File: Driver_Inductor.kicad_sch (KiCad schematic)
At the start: 6 parts, among them J1 2-338069-0, J2 DC+, J3 DC-, J4 OUT1, J5 OUT2

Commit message: Тестовая версия
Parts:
- J2, J3: footprint Connector Power:M4 -> Connector_Power:M5
- J4, J5: footprint Connector Power:M5 -> Connector_Power:M5
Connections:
- net Current_N is gone; now on net +15V: J1.8
- net Current_P is gone; now on net GND: J1.7
- net +15V: now also J1.10; no longer J1.18, J1.2
- net DESAT_H: now also D20.25 (DC+), D20.26 (DC+), J2.1 (Pin_1); no longer D20.15 (DC+)
- net E3: no longer D20.21 (OUT2), D20.22 (OUT2), J5.1 (Pin_1)
- net Fault_N: now also J1.1; no longer J1.10
- net Fault_P: now also J1.2; no longer J1.9
- net GND: now also J1.9; no longer J1.1
- net PWM1_N: now also J1.14; no longer J1.16
- net PWM1_P: now also J1.13; no longer J1.15
- net PWM2_N: now also J1.16; no longer J1.14
- net PWM2_P: now also J1.15; no longer J1.13
- net Reset: now also J1.18; no longer J1.20
- net Temp_N: now also J1.11; no longer J1.12
- net Temp_P: now also J1.12; no longer J1.11
- net E1 renamed OUT1
- new net Current: J1.20
- new net OUT2: D20.21 (OUT2), D20.22 (OUT2)
- new net OUT2_Sens: J5.1 (Pin_1)
- no-connect marks 5 -> 6
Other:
- moved on the sheet: J5

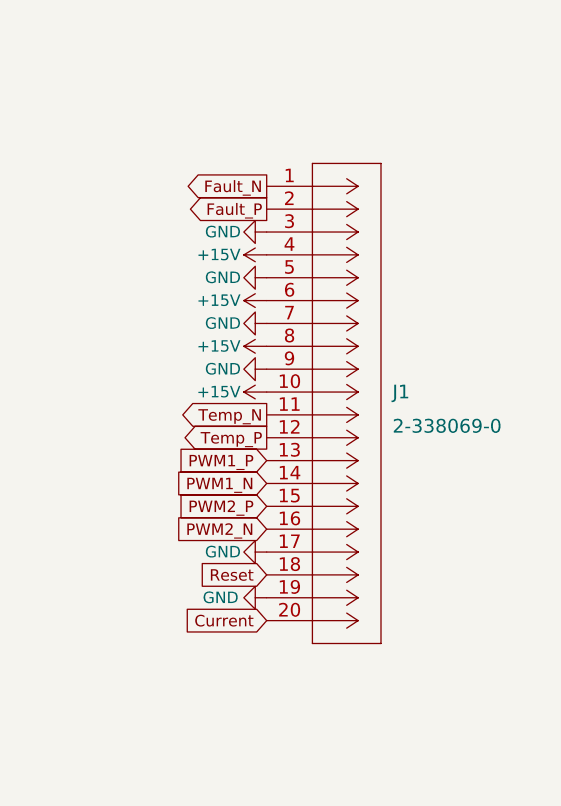
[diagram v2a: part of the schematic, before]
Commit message: Убрал питание 3.3В
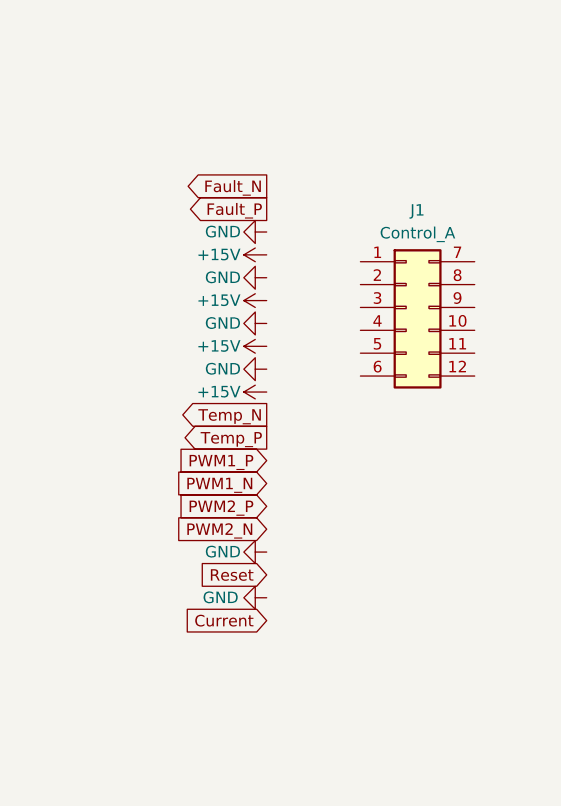
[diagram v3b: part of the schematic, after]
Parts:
- removed J1: 2-338069-0, Connector_My:2-338069-0, symbol Connector_My:2-338069-0
- added J1: Control_A, Connector_Molex:Molex_Micro-Fit_3.0_43045-1212_2x06_P3.00mm_Vertical, symbol Connector_Generic:Conn_02x06_Top_Bottom

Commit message: Развел все дорожки
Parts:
- added C10: 1u, Capacitor_THT:C_Rect_L31.5mm_W13.0mm_P27.50mm_MKS4, symbol Device:C
- J2, J3, J4, J5: footprint Connector_Power:M5 -> Connector_My:Bush_M4
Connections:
- net +15V: now also J1.2 (Pin_2)
- net Current: now also J1.12 (Pin_12)
- net Fault_N: now also J1.10 (Pin_10)
- net Fault_P: now also J1.4 (Pin_4)
- net GND: now also J1.8 (Pin_8)
- net PWM1_N: now also J1.9 (Pin_9)
- net PWM1_P: now also J1.3 (Pin_3)
- net PWM2_N: now also J1.11 (Pin_11)
- net PWM2_P: now also J1.5 (Pin_5)
- net Reset: now also J1.6 (Pin_6)
- net Temp_N: now also J1.1 (Pin_1)
- net Temp_P: now also J1.7 (Pin_7)
- net DC-: now reaches D20.27 (DC-), D20.28 (DC-), J3.1 (Pin_1)
- net DC-: now also C10.2
- net DESAT_H renamed DC+
- net DC+: now also C10.1
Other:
- moved on the sheet: J1, J2, J3

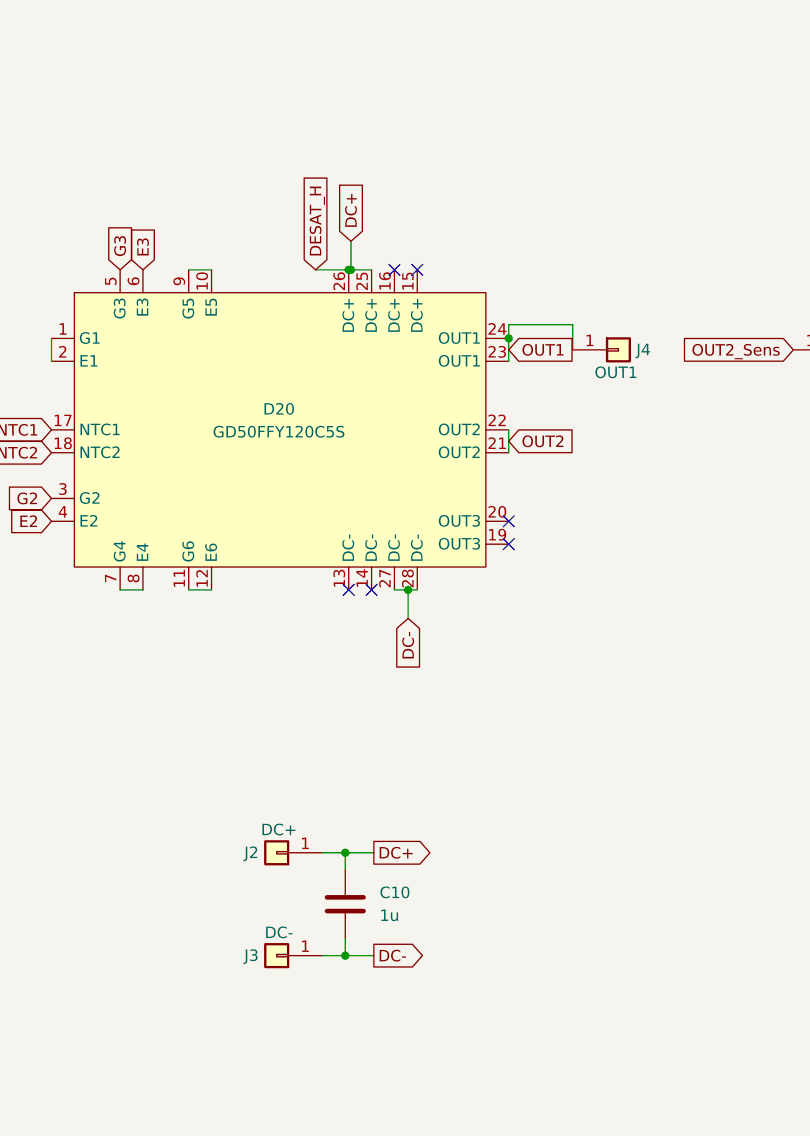
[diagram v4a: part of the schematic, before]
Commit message: Заменил в схеме символы питания
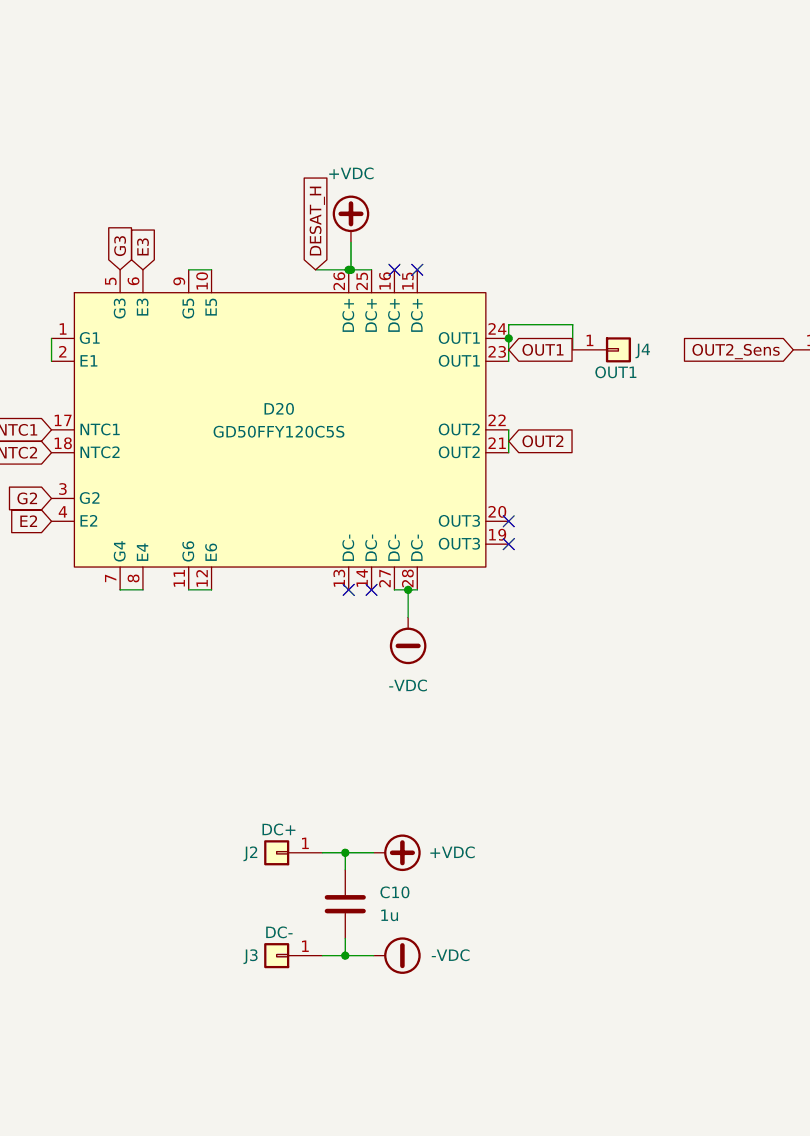
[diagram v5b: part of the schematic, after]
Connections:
- net DC+ renamed +VDC
- net DC- renamed -VDC

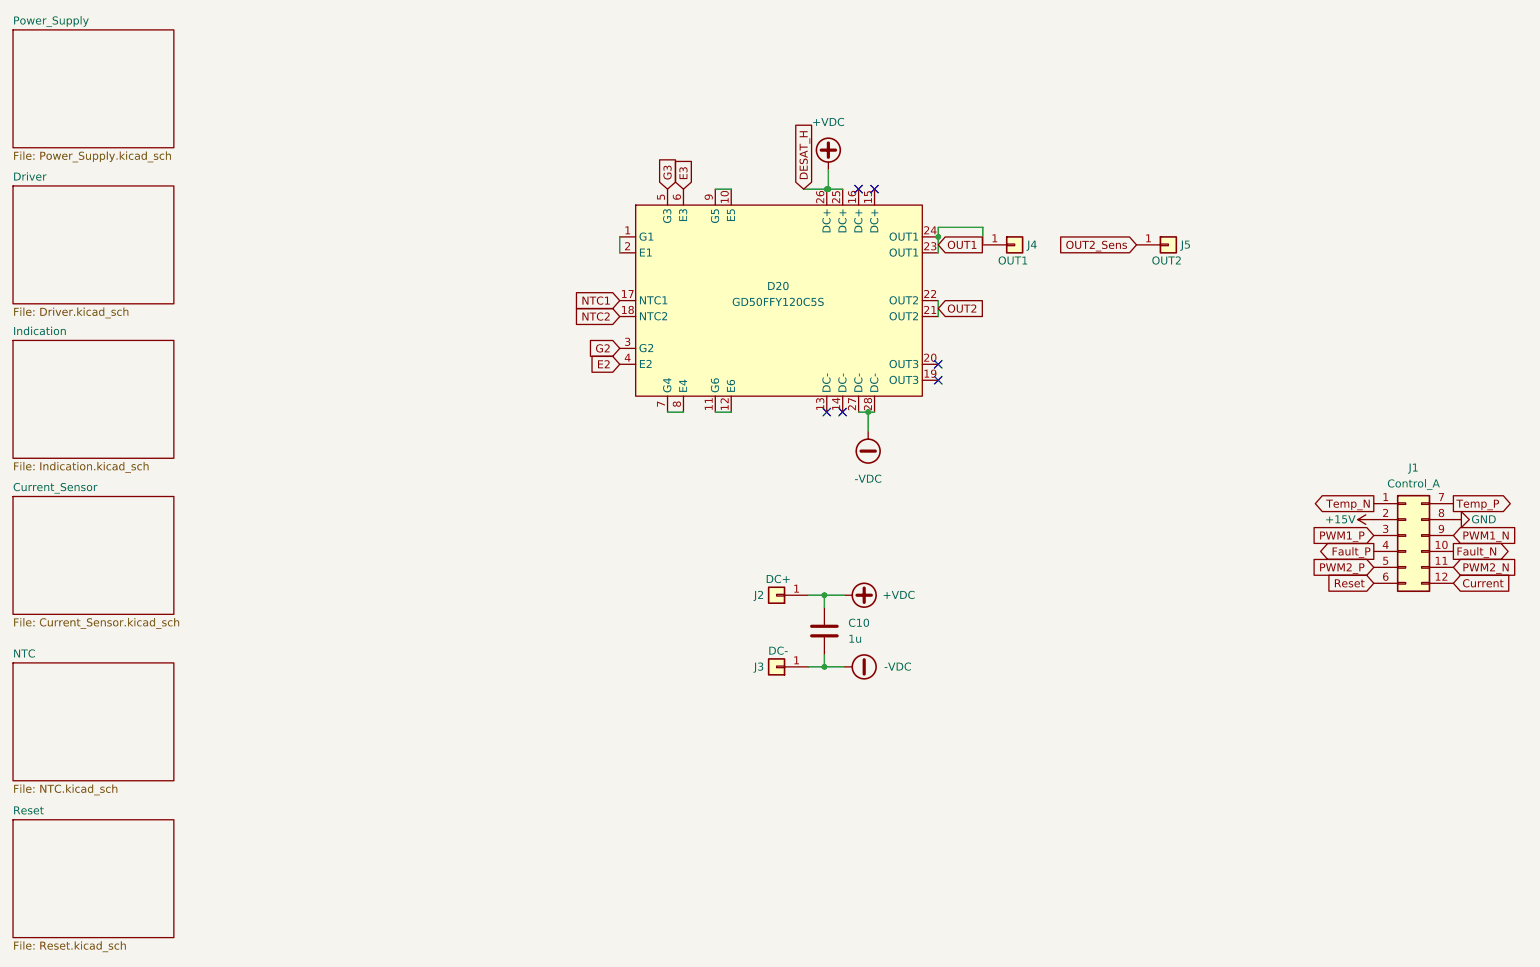
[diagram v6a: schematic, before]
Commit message: VER2.1: внес все исправления для заказа в Китае
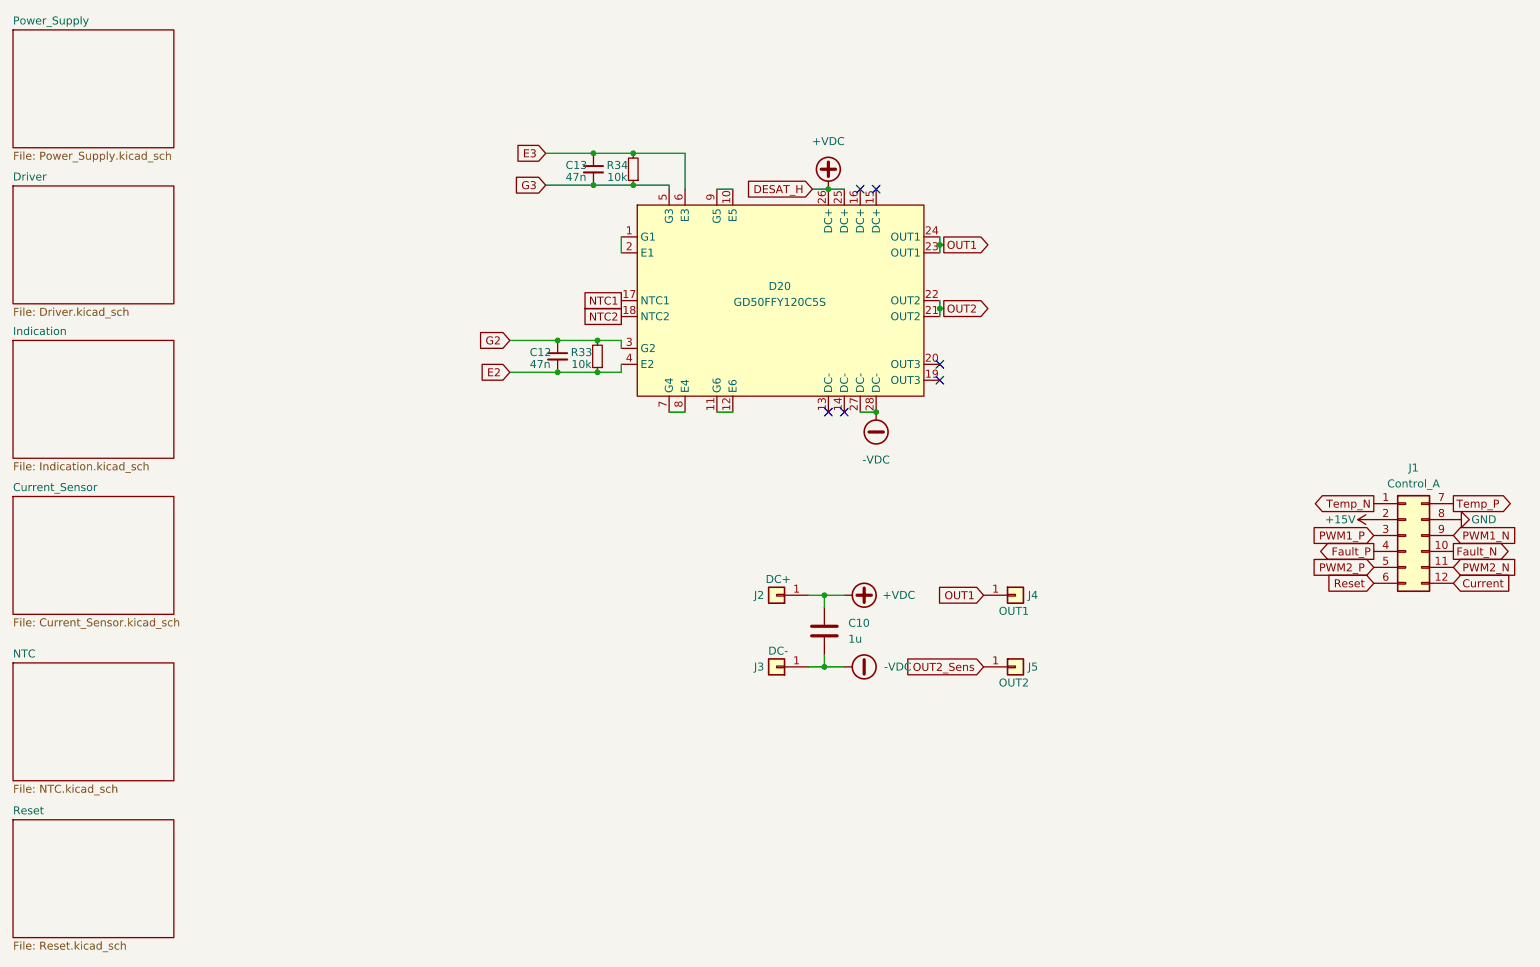
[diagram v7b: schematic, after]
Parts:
- added C12, C13: 47n, Capacitor_SMD:C_0805_2012Metric_Pad1.18x1.45mm_HandSolder, symbol Device:C_Small
- added R33, R34: 10k, Resistor_SMD:R_0805_2012Metric_Pad1.20x1.40mm_HandSolder, symbol Device:R_Small
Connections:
- net E2: now also C12.2, R33.1
- net E3: now also C13.1, R34.2
- net G2: now also C12.1, R33.2
- net G3: now also C13.2, R34.1
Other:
- moved on the sheet: J4, J5

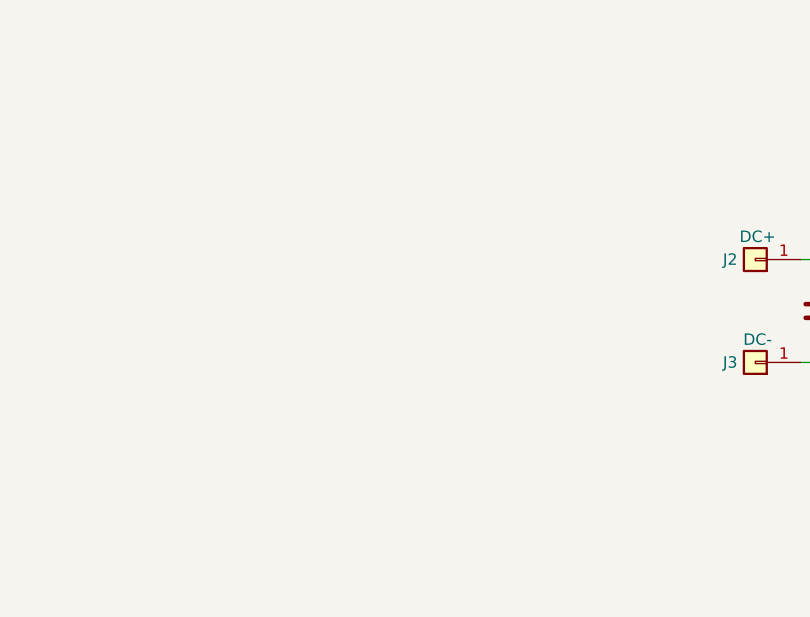
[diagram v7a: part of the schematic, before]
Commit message: VER2.2: добавил цепь подавления колебаний
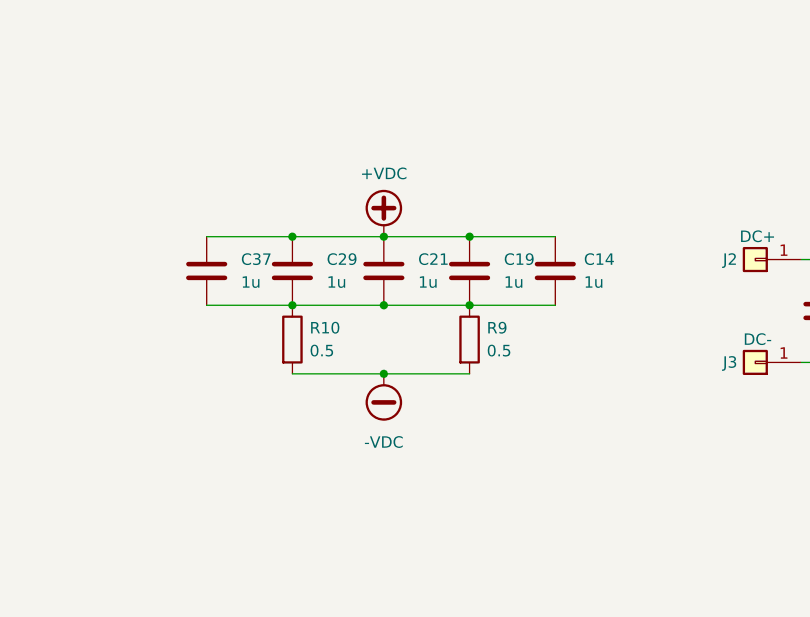
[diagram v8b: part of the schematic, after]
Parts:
- added C14, C19, C21, C29, C37: 1u, Capacitor_SMD:C_2220_5750Metric_Pad1.97x5.40mm_HandSolder, symbol Device:C
- added R10, R9: 0.5, Resistor_SMD:R_2512_6332Metric_Pad1.40x3.35mm_HandSolder, symbol Device:R
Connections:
- net +VDC: now also C14.1, C19.1, C21.1, C29.1, C37.1
- net -VDC: now also R10.2, R9.2
- new net: C14.2, C19.2, C21.2, C29.2, C37.2, R10.1, R9.1
